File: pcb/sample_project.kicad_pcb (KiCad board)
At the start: 2 copper layers, 20 x 10 mm, 1 part

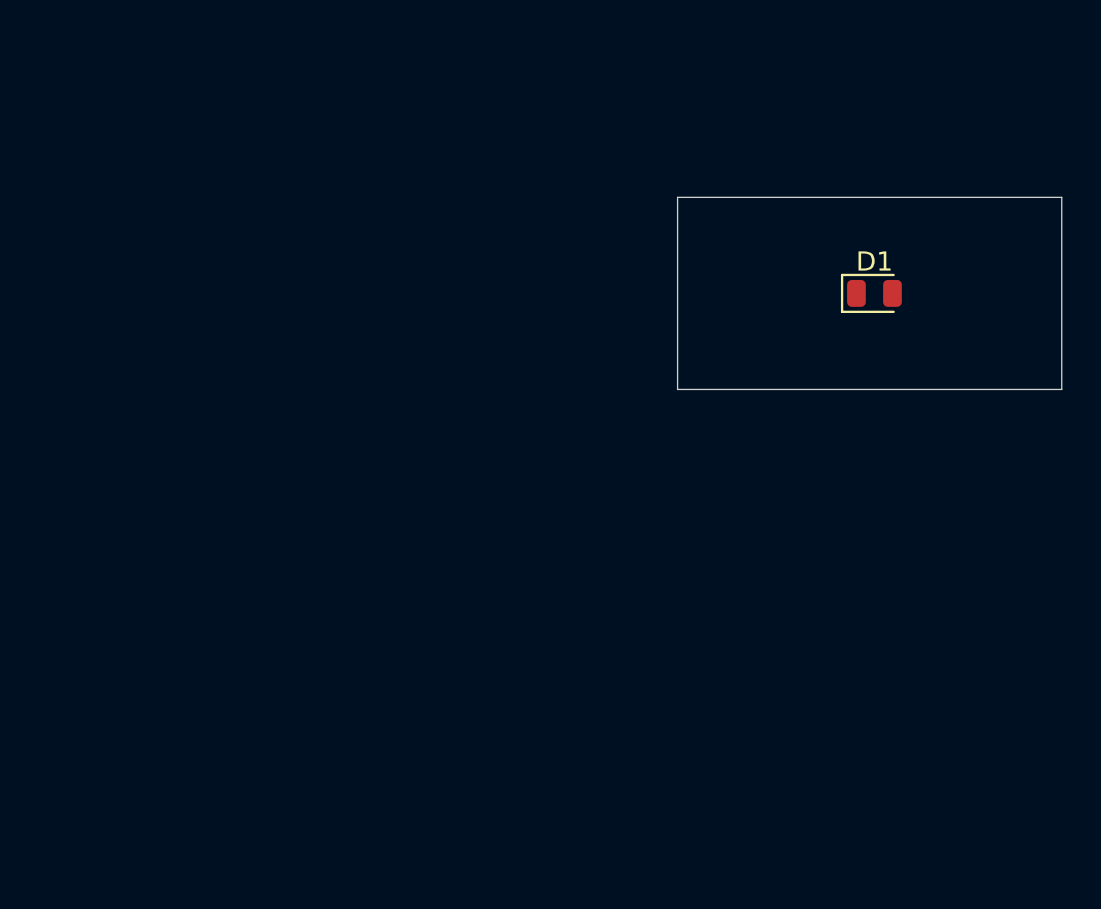
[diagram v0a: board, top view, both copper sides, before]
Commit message: Updated exporting script
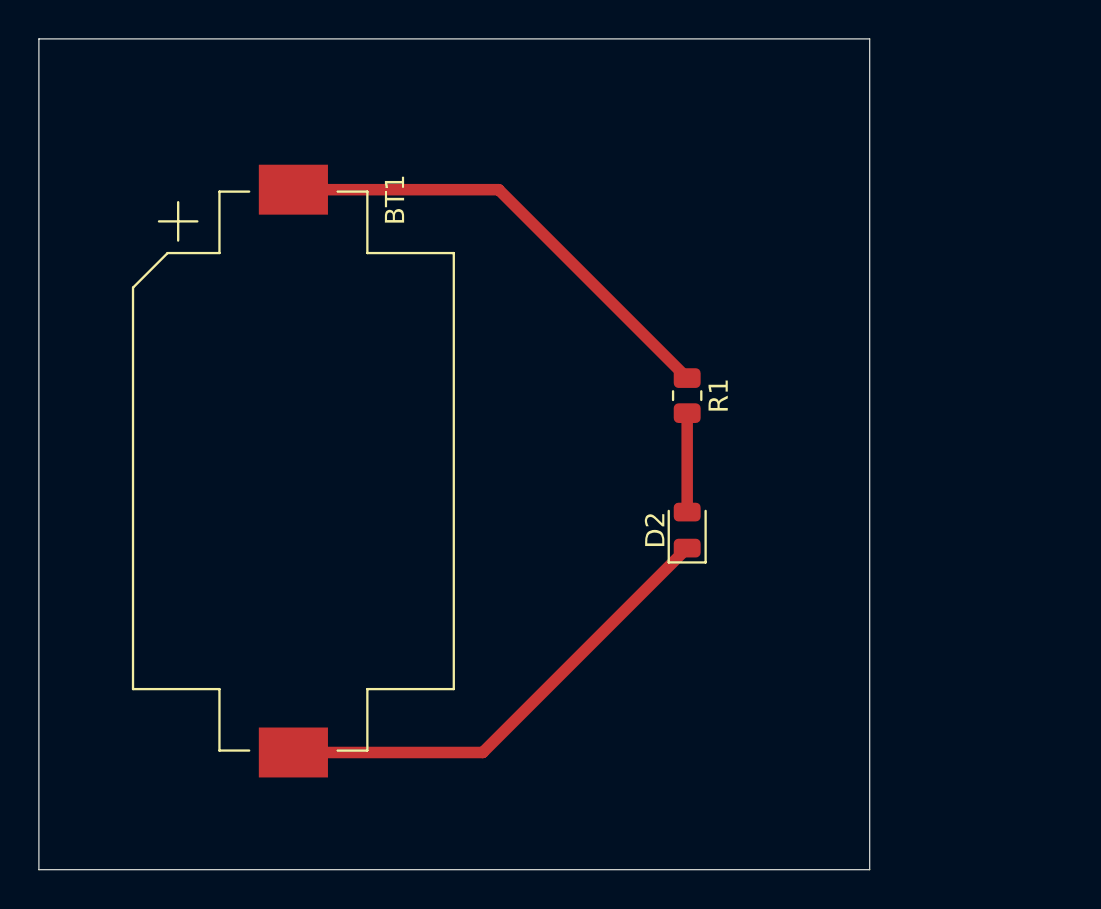
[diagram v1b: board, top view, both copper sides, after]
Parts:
- removed D1: LED, LED_SMD:LED_0805_2012Metric
- added BT1: Battery_Cell, Battery:BatteryHolder_Keystone_1060_1x2032, F.Cu at (119.8, 108.8)
- added D2: LED_Small, LED_SMD:LED_0805_2012Metric, F.Cu at (140.2, 111.8)
- added R1: R_Small, Resistor_SMD:R_0805_2012Metric, F.Cu at (140.2, 104.8)
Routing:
- net GND: track 0.00 -> 24.9 mm
- net +BATT: track 0.00 -> 24.6 mm
- net Net-(D2-A): track 0.00 -> 5.15 mm
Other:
- board size 20 x 10 mm -> 43.2 x 43.2 mm
